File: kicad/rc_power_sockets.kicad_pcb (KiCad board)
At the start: 2 copper layers, 50 x 50 mm, 24 parts, among them IC1 ATTINY85, J1 PIR, J2 433MHZ, J3 433MHZ, P1 ICSP, P2 CONN_GND, Q1 NMOS, Q2 PMOS, SW1 SPST, U1 MCP1700T

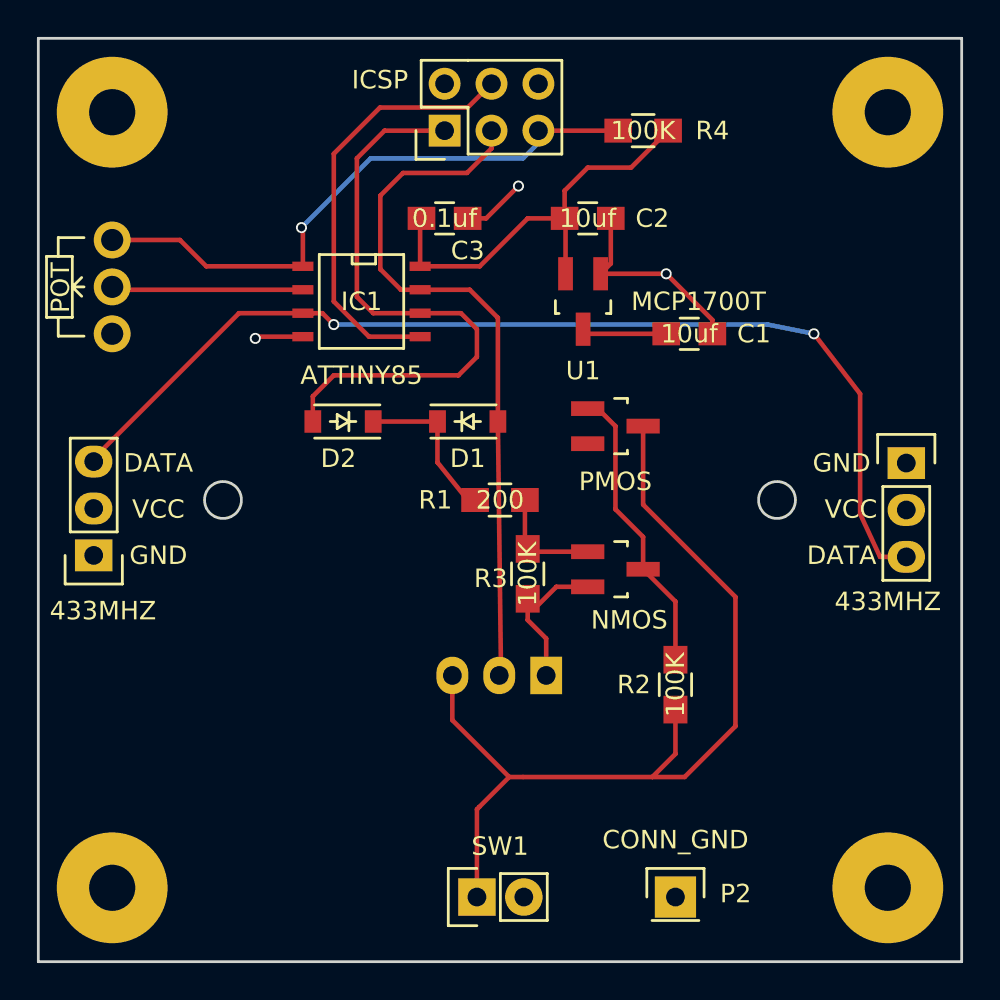
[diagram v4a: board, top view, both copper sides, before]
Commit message: Moved silkscreens
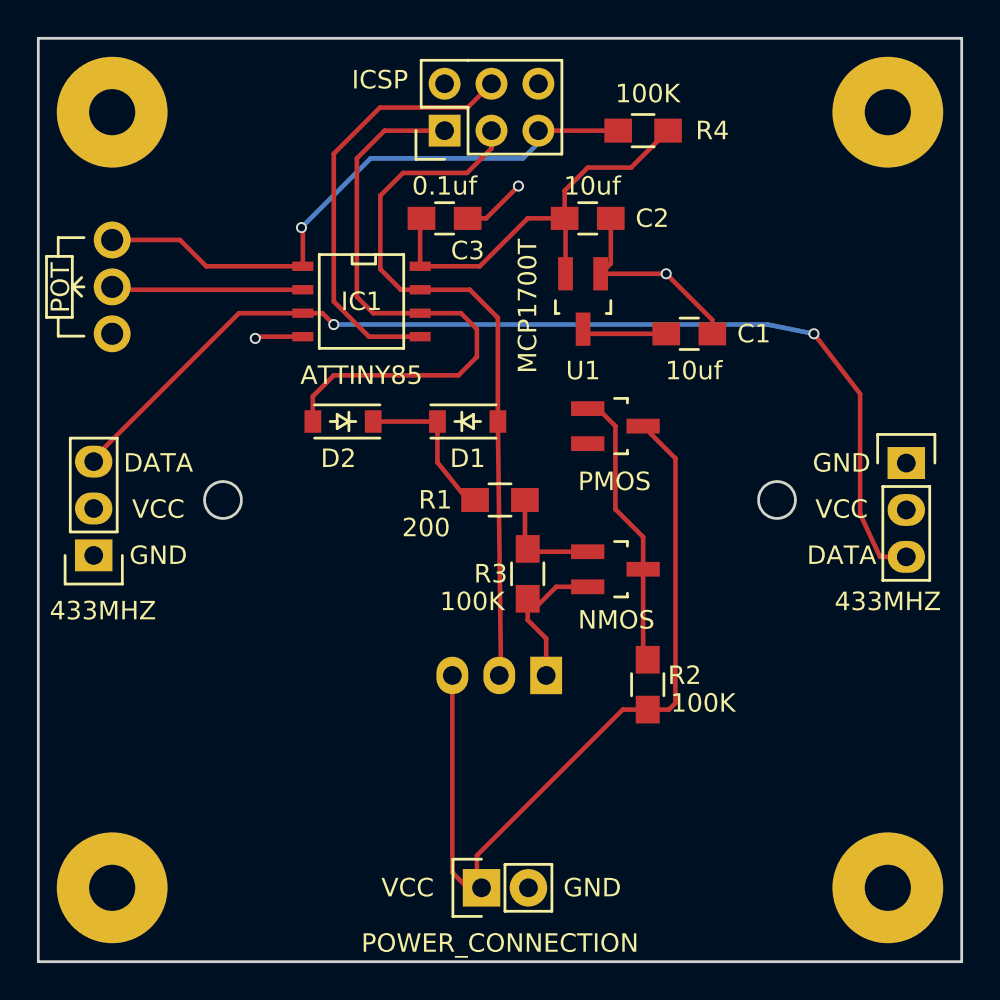
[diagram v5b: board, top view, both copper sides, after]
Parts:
- removed SW1: SPST, Pin_Headers:Pin_Header_Straight_1x02
- P2: value CONN_GND -> POWER_CONNECTION; footprint Pin_Headers:Pin_Header_Straight_1x01 -> Pin_Headers:Pin_Header_Straight_1x02
- moved P2 10.5 mm to (144.0, 106.0), turned to 90 degrees
- moved R2 1.50 mm to (153.0, 95.0)
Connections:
- J1 pad 3: /POWER -> VCC
- P2 pad 1: GND -> VCC
- Q2 pad 3: /POWER -> VCC
- R2 pad 1: /POWER -> VCC
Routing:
- net /POWER: track 49.9 -> 0.00 mm
- net VCC: track 0.00 -> 44.7 mm
- net /PBASE: track 15.9 -> 15.3 mm

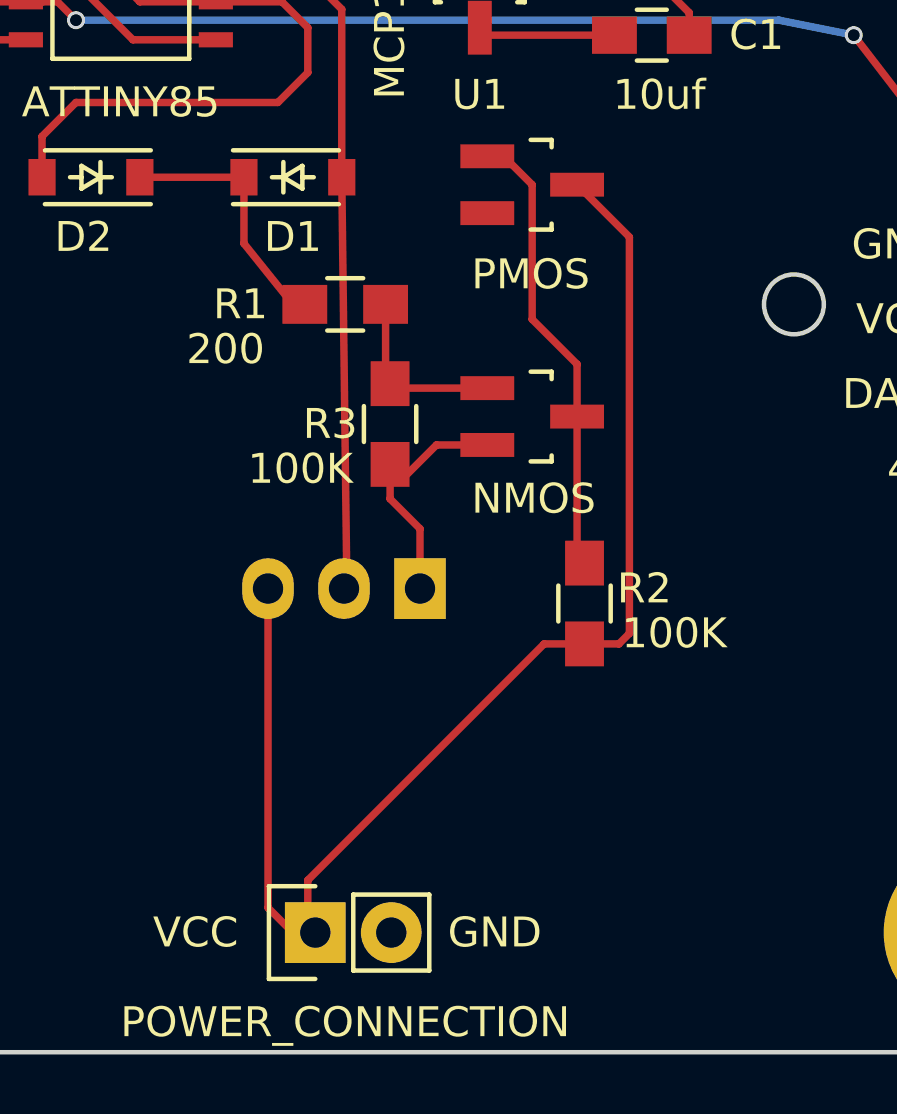
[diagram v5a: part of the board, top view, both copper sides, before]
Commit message: Wider VCC trace
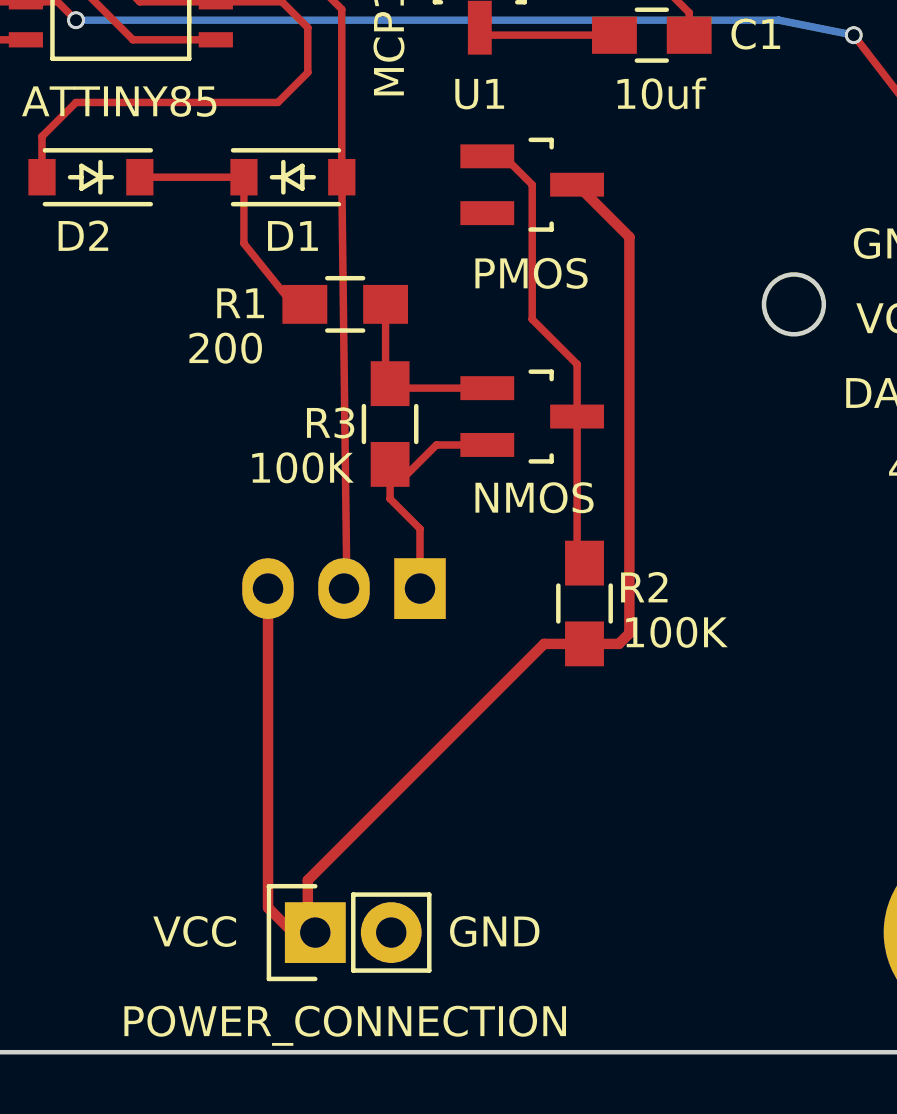
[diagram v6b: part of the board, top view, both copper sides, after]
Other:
- net class VCC added: clearance 0.3, trace_width 0.35, via_dia 0.6, via_drill 0.4
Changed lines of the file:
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@@
     (links 46)
     (no_connects 0)
-    (area 119.924999 59.924999 170.075001 110.075001)
+    (area 118.275 59.924999 172.478334 112.155)
     (thickness 1.6)
     (drawings 17)
@@
     (add_net /SWITCH_POWER)
     (add_net GND)
+  )
+  (net_class VCC ""
+    (clearance 0.3)
+    (trace_width 0.35)
+    (via_dia 0.6)
+    (via_drill 0.4)
+    (uvia_dia 0.3)
+    (uvia_drill 0.1)
     (add_net VCC)
   )
@@
   (segment (start 134.325 73.615) (end 124.155 73.615) (width 0.25) (layer F.Cu) (net 7))
   (segment (start 124.155 73.615) (end 124 73.46) (width 0.25) (layer F.Cu) (net 7))
-  (segment (start 153 96.35) (end 151.65 96.35) (width 0.25) (layer F.Cu) (net 8))
-  (segment (start 151.65 96.35) (end 143.75 104.25) (width 0.25) (layer F.Cu) (net 8))
-  (segment (start 142.42 94.5) (end 142.42 105.17) (width 0.25) (layer F.Cu) (net 8))
-  (segment (start 142.42 105.17) (end 143.75 106.5) (width 0.25) (layer F.Cu) (net 8))
-  (segment (start 153 96.35) (end 154.15 96.35) (width 0.25) (layer F.Cu) (net 8))
-  (segment (start 154.5 82.74886) (end 152.75114 81) (width 0.25) (layer F.Cu) (net 8))
-  (segment (start 154.5 96) (end 154.5 82.74886) (width 0.25) (layer F.Cu) (net 8))
-  (segment (start 154.15 96.35) (end 154.5 96) (width 0.25) (layer F.Cu) (net 8))
-  (segment (start 143.75 104.25) (end 143.75 106.5) (width 0.25) (layer F.Cu) (net 8))
+  (segment (start 153 96.35) (end 151.65 96.35) (width 0.35) (layer F.Cu) (net 8))
+  (segment (start 143.75 104.25) (end 143.75 106.5) (width 0.35) (layer F.Cu) (net 8))
+  (segment (start 151.65 96.35) (end 143.75 104.25) (width 0.35) (layer F.Cu) (net 8))
+  (segment (start 142.42 94.5) (end 142.42 105.17) (width 0.35) (layer F.Cu) (net 8))
+  (segment (start 142.42 105.17) (end 143.75 106.5) (width 0.35) (layer F.Cu) (net 8))
+  (segment (start 153 96.35) (end 154.15 96.35) (width 0.35) (layer F.Cu) (net 8))
+  (segment (start 154.15 96.35) (end 154.5 96) (width 0.35) (layer F.Cu) (net 8))
+  (segment (start 154.5 96) (end 154.5 82.74886) (width 0.35) (layer F.Cu) (net 8))
+  (segment (start 154.5 82.74886) (end 152.75114 81) (width 0.35) (layer F.Cu) (net 8))
   (segment (start 154 76) (end 149.74886 76) (width 0.25) (layer F.Cu) (net 9))
   (segment (start 149.74886 76) (end 149.5 75.75114) (width 0.25) (layer F.Cu) (net 9))

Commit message: Logo
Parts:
- added REF**: TheApiLogo, theapi_footprints:TheApiLogo, F.Cu at (133.2, 84.8)
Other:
- board text added: "RC Power Sockets v1.0"
- board text added: "www.theapi.co.uk"
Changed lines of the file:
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@@
     (links 46)
     (no_connects 0)
-    (area 118.275 59.924999 172.478334 112.155)
+    (area 119.924999 59.924999 170.075001 110.075001)
     (thickness 1.6)
-    (drawings 17)
+    (drawings 19)
     (tracks 112)
     (zones 0)
-    (modules 23)
+    (modules 24)
     (nets 14)
   )
@@
   (layers
     (0 F.Cu signal)
-    (31 B.Cu signal hide)
+    (31 B.Cu signal)
     (32 B.Adhes user)
     (33 F.Adhes user)
@@
     )
   )
+  (module theapi_footprints:TheApiLogo (layer F.Cu)
+    (at 133.2 84.8)
+    (fp_text reference REF** (at -1.45 16.875) (layer F.SilkS) hide
+      (effects (font (size 1 1) (thickness 0.15)))
+    )
+    (fp_text value TheApiLogo (at 0 -0.5) (layer F.Fab) hide
+      (effects (font (size 1 1) (thickness 0.15)))
+    )
+    (fp_line (start 2.575 21.95) (end 3.3 20.725) (layer F.SilkS) (width 0.15))
+    (fp_line (start 3.3 20.725) (end 3.55 19.725) (layer F.SilkS) (width 0.15))
+    (fp_line (start 3.55 19.725) (end 3.925 21.25) (layer F.SilkS) (width 0.15))
+    (fp_line (start 3.925 21.25) (end 3.375 22.325) (layer F.SilkS) (width 0.15))
+    (fp_line (start 3.375 22.325) (end 2.5 23.475) (layer F.SilkS) (width 0.15))
+    (fp_line (start 2.5 23.475) (end 2.85 23.3) (layer F.SilkS) (width 0.15))
+    (fp_line (start 0.35 9.95) (end 1.25 12.275) (layer F.SilkS) (width 0.15))
+    (fp_line (start 1.25 12.275) (end 2.05 13.5) (layer F.SilkS) (width 0.15))
+    (fp_line (start 2.05 13.5) (end 2.575 15.025) (layer F.SilkS) (width 0.15))
+    (fp_line (start 2.575 15.025) (end 2.85 16.725) (layer F.SilkS) (width 0.15))
+    (fp_line (start 2.85 16.725) (end 2.95 18.575) (layer F.SilkS) (width 0.15))
+    (fp_line (start 2.95 18.575) (end 2.675 20.625) (layer F.SilkS) (width 0.15))
+    (fp_line (start 2.675 20.625) (end 2.5 23.025) (layer F.SilkS) (width 0.15))
+    (fp_line (start 2.5 23.025) (end 2.05 24.525) (layer F.SilkS) (width 0.15))
+    (fp_line (start 2.05 24.525) (end 2.05 24.9) (layer F.SilkS) (width 0.15))
+    (fp_line (start -1.025 7.525) (end -0.7 8.05) (layer F.SilkS) (width 0.15))
+    (fp_line (start -0.7 8.05) (end -0.25 8.25) (layer F.SilkS) (width 0.15))
+    (fp_line (start -0.25 8.25) (end 0.325 8.475) (layer F.SilkS) (width 0.15))
+    (fp_line (start 0.325 8.475) (end 1.1 8.6) (layer F.SilkS) (width 0.15))
+    (fp_line (start 1.1 8.6) (end 1.725 8.375) (layer F.SilkS) (width 0.15))
+    (fp_line (start 1.725 8.375) (end 2.15 7.975) (layer F.SilkS) (width 0.15))
+    (fp_line (start 2.15 7.975) (end 2.325 7.3) (layer F.SilkS) (width 0.15))
+    (fp_line (start 2.325 7.3) (end 2.225 7.3) (layer F.SilkS) (width 0.15))
+    (fp_line (start 1.55 5.7) (end 1.05 5.75) (layer F.SilkS) (width 0.15))
+    (fp_line (start 1.05 5.75) (end 0.925 6.075) (layer F.SilkS) (width 0.15))
+    (fp_line (start 0.925 6.075) (end 0.975 6.525) (layer F.SilkS) (width 0.15))
+    (fp_line (start 0.975 6.525) (end 1.6 6.575) (layer F.SilkS) (width 0.15))
+    (fp_line (start 1.6 6.575) (end 1.875 6.3) (layer F.SilkS) (width 0.15))
+    (fp_line (start 1.875 6.3) (end 1.55 5.975) (layer F.SilkS) (width 0.15))
+    (fp_line (start -0.7 5.7) (end -1.025 5.925) (layer F.SilkS) (width 0.15))
+    (fp_line (start -1.025 5.925) (end -1.025 6.575) (layer F.SilkS) (width 0.15))
+    (fp_line (start -1.025 6.575) (end -0.475 6.575) (layer F.SilkS) (width 0.15))
+    (fp_line (start -0.475 6.575) (end -0.075 6.425) (layer F.SilkS) (width 0.15))
+    (fp_line (start -0.075 6.425) (end -0.125 6.025) (layer F.SilkS) (width 0.15))
+    (fp_line (start -0.125 6.025) (end -0.4 5.975) (layer F.SilkS) (width 0.15))
+    (fp_line (start -0.4 5.975) (end -0.7 5.8) (layer F.SilkS) (width 0.15))
+    (fp_line (start -0.7 5.8) (end -0.4 5.8) (layer F.SilkS) (width 0.15))
+    (fp_line (start 4.05 9.5) (end 3.625 9) (layer F.SilkS) (width 0.15))
+    (fp_line (start 3.625 9) (end 2.725 8.6) (layer F.SilkS) (width 0.15))
+    (fp_line (start 2.725 8.6) (end 3.825 8.6) (layer F.SilkS) (width 0.15))
+    (fp_line (start 3.825 8.6) (end 5.3 8.15) (layer F.SilkS) (width 0.15))
+    (fp_line (start 5.3 8.15) (end 6.175 7.6) (layer F.SilkS) (width 0.15))
+    (fp_line (start 6.175 7.6) (end 6.475 6.8) (layer F.SilkS) (width 0.15))
+    (fp_line (start 6.475 6.8) (end 6.4 6.15) (layer F.SilkS) (width 0.15))
+    (fp_line (start 6.4 6.15) (end 6.125 5.7) (layer F.SilkS) (width 0.15))
+    (fp_line (start 6.125 5.7) (end 5.45 5.25) (layer F.SilkS) (width 0.15))
+    (fp_line (start 5.45 5.25) (end 4.775 5.2) (layer F.SilkS) (width 0.15))
+    (fp_line (start 4.775 5.2) (end 3.9 5.125) (layer F.SilkS) (width 0.15))
+    (fp_line (start 3.9 5.125) (end 3.225 5.125) (layer F.SilkS) (width 0.15))
+    (fp_line (start 3.225 5.125) (end 2.825 5.125) (layer F.SilkS) (width 0.15))
+    (fp_line (start 2.825 5.125) (end 2.825 5.075) (layer F.SilkS) (width 0.15))
+    (fp_line (start -2.15 5.575) (end -3.15 5.75) (layer F.SilkS) (width 0.15))
+    (fp_line (start -3.15 5.75) (end -3.875 5.925) (layer F.SilkS) (width 0.15))
+    (fp_line (start -3.875 5.925) (end -4.65 6.35) (layer F.SilkS) (width 0.15))
+    (fp_line (start -4.65 6.35) (end -5.325 6.925) (layer F.SilkS) (width 0.15))
+    (fp_line (start -5.325 6.925) (end -5.45 8.1) (layer F.SilkS) (width 0.15))
+    (fp_line (start -5.45 8.1) (end -5 9) (layer F.SilkS) (width 0.15))
+    (fp_line (start -5 9) (end -4.15 9.375) (layer F.SilkS) (width 0.15))
+    (fp_line (start -4.15 9.375) (end -3.1 9.275) (layer F.SilkS) (width 0.15))
+    (fp_line (start -3.1 9.275) (end -2.475 8.875) (layer F.SilkS) (width 0.15))
+    (fp_line (start -2.475 8.875) (end -2.025 8.6) (layer F.SilkS) (width 0.15))
+    (fp_line (start -2.025 8.6) (end -2.525 9.325) (layer F.SilkS) (width 0.15))
+    (fp_line (start -2.525 9.325) (end -2.925 10.55) (layer F.SilkS) (width 0.15))
+    (fp_line (start -2.925 10.55) (end -2.7 11.45) (layer F.SilkS) (width 0.15))
+    (fp_line (start -2.7 11.45) (end -2.2 12.225) (layer F.SilkS) (width 0.15))
+    (fp_line (start -2.2 12.225) (end -1.35 12.35) (layer F.SilkS) (width 0.15))
+    (fp_line (start -1.35 12.35) (end -0.175 12.125) (layer F.SilkS) (width 0.15))
+    (fp_line (start -0.175 12.125) (end 0.25 11.5) (layer F.SilkS) (width 0.15))
+    (fp_line (start 0.25 11.5) (end 0.425 10.775) (layer F.SilkS) (width 0.15))
+    (fp_line (start 0.425 10.775) (end 0.375 9.95) (layer F.SilkS) (width 0.15))
+    (fp_line (start 0.375 9.95) (end 0.825 10.675) (layer F.SilkS) (width 0.15))
+    (fp_line (start 0.825 10.675) (end 1.275 11.225) (layer F.SilkS) (width 0.15))
+    (fp_line (start 1.275 11.225) (end 2.375 11.85) (layer F.SilkS) (width 0.15))
+    (fp_line (start 2.375 11.85) (end 3.5 11.775) (layer F.SilkS) (width 0.15))
+    (fp_line (start 3.5 11.775) (end 4.4 11) (layer F.SilkS) (width 0.15))
+    (fp_line (start 4.4 11) (end 4.45 10.15) (layer F.SilkS) (width 0.15))
+    (fp_line (start 4.45 10.15) (end 4 9.425) (layer F.SilkS) (width 0.15))
+    (fp_line (start 0.425 3.95) (end -0.025 3.175) (layer F.SilkS) (width 0.15))
+    (fp_line (start -0.025 3.175) (end -0.7 2.625) (layer F.SilkS) (width 0.15))
+    (fp_line (start -0.7 2.625) (end -1.475 2.125) (layer F.SilkS) (width 0.15))
+    (fp_line (start -1.475 2.125) (end -2.875 2) (layer F.SilkS) (width 0.15))
+    (fp_line (start -2.875 2) (end -3.775 2.45) (layer F.SilkS) (width 0.15))
+    (fp_line (start -3.775 2.45) (end -4.325 3.3) (layer F.SilkS) (width 0.15))
+    (fp_line (start -4.325 3.3) (end -4.275 4.3) (layer F.SilkS) (width 0.15))
+    (fp_line (start -4.275 4.3) (end -3.65 5.125) (layer F.SilkS) (width 0.15))
+    (fp_line (start -3.65 5.125) (end -2.875 5.3) (layer F.SilkS) (width 0.15))
+    (fp_line (start -2.875 5.3) (end -2.025 5.475) (layer F.SilkS) (width 0.15))
+    (fp_line (start -2.025 5.475) (end -2.075 5.7) (layer F.SilkS) (width 0.15))
+    (fp_line (start 0.475 3.95) (end 0.65 2.9) (layer F.SilkS) (width 0.15))
+    (fp_line (start 0.65 2.9) (end 1.15 2) (layer F.SilkS) (width 0.15))
+    (fp_line (start 1.15 2) (end 2.375 1.325) (layer F.SilkS) (width 0.15))
+    (fp_line (start 2.375 1.325) (end 3.775 1.45) (layer F.SilkS) (width 0.15))
+    (fp_line (start 3.775 1.45) (end 4.625 2.225) (layer F.SilkS) (width 0.15))
+    (fp_line (start 4.625 2.225) (end 4.85 3.35) (layer F.SilkS) (width 0.15))
+    (fp_line (start 4.85 3.35) (end 4.225 4.3) (layer F.SilkS) (width 0.15))
+    (fp_line (start 4.225 4.3) (end 3.4 4.9) (layer F.SilkS) (width 0.15))
+    (fp_line (start 3.4 4.9) (end 2.775 5.125) (layer F.SilkS) (width 0.15))
+    (fp_circle (center 0.4 6.87) (end 2.94 5.6) (layer F.SilkS) (width 0.15))
+  )
+  (gr_text www.theapi.co.uk (at 144.8 82.6) (layer B.SilkS)
+    (effects (font (size 1 1) (thickness 0.15)) (justify mirror))
+  )
+  (gr_text "RC Power Sockets v1.0" (at 145 80.6) (layer B.SilkS)
+    (effects (font (size 1 1) (thickness 0.15) italic) (justify mirror))
+  )
   (gr_text VCC (at 140 106) (layer F.SilkS)
